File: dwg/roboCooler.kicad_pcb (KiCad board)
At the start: 2 copper layers, 60 x 72 mm, 62 parts, among them J1 CONN_01X02, J10 CONN_02X03, J11 CONN_01X04, J12 USB_A, J13 CONN_02X03, J14 CONN_02X03, J2 CONN_01X02, J3 Discovery_F407_P1, J4 CONN_01X06, J5 CONN_01X12, J6 Discovery_F407_P2, J7 CONN_02X03, J8 CONN_02X03, Q1 NMOS, Q2 NMOS, U1 SN74LV, U2 TB6549

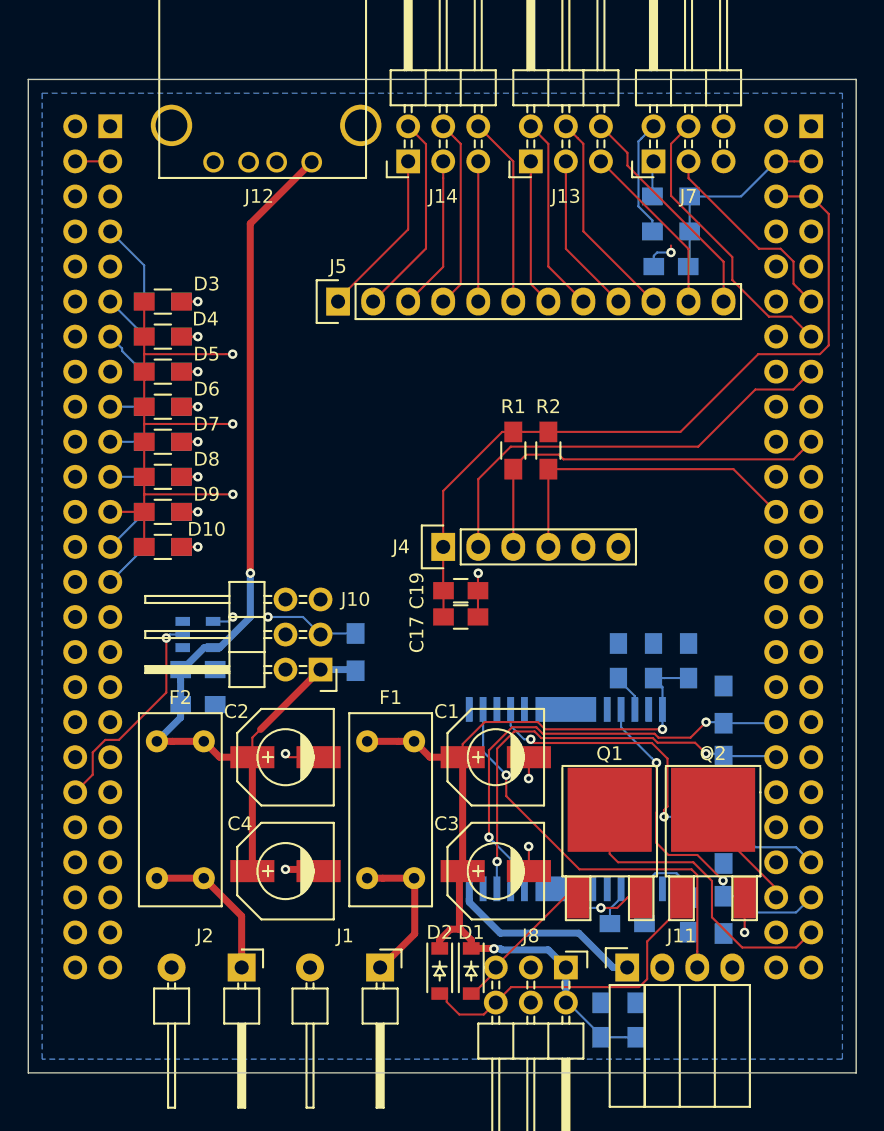
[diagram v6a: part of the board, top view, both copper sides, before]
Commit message: increased some track widths on pcb
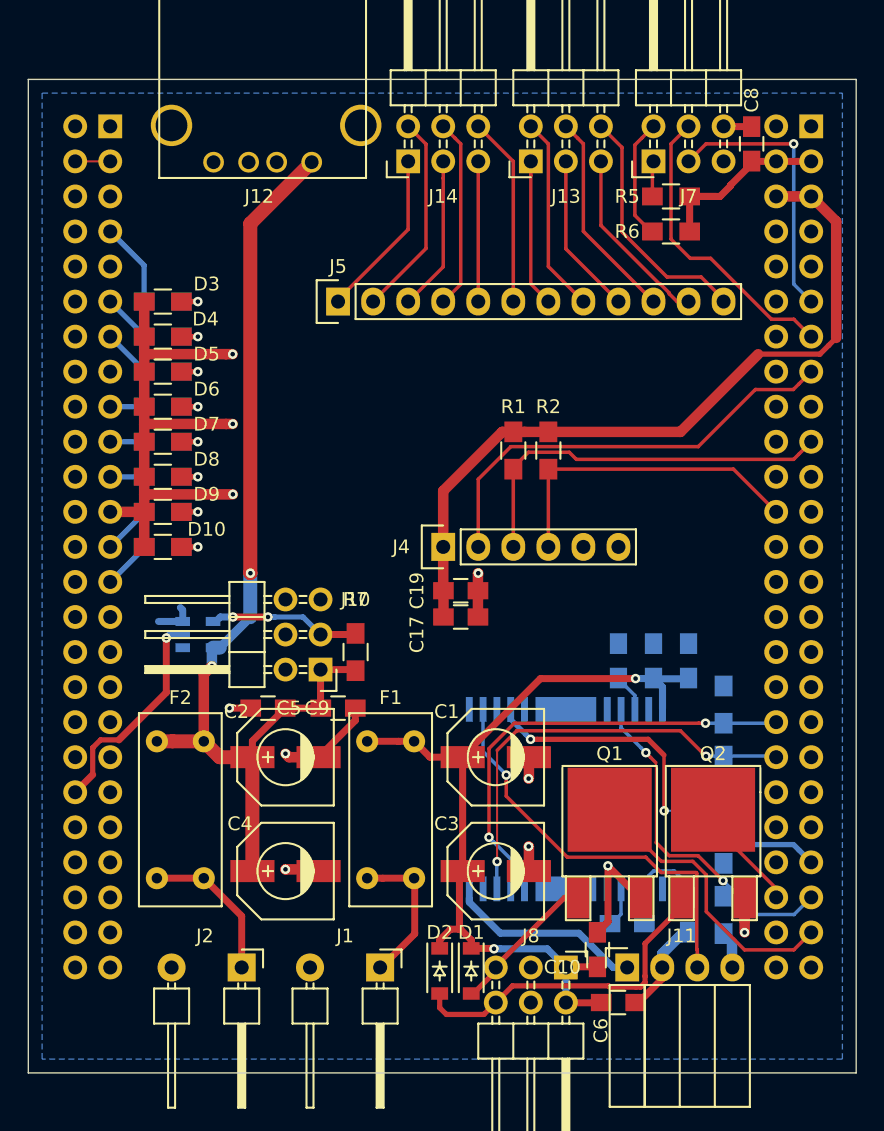
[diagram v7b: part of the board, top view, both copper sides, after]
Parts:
- C10, C5, C6, C8, C9, R5, R6, R7: moved to F.Cu
- moved C8 10.6 mm to (74.4, 26.7), turned to 90 degrees
- moved C5 10.5 mm to (44.5, 67.6)
- moved C10 5.82 mm to (63.2, 85.1)
- moved C9 5.09 mm to (39.4, 67.6), turned to 180 degrees
- moved C6 1.80 mm to (64.8, 88.9), turned to 0 degrees
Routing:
- net GND: track 64.1 -> 82.9 mm
- net HALL_1: track 14.8 -> 20.1 mm, vias 0 -> 1
- net FAN: track 22.6 -> 20.9 mm
- net CS_0: track 16.4 -> 17.8 mm
- net PUMP: track 8.25 -> 7.12 mm
- net Net-(D2-Pad2): track 23.9 -> 24.8 mm
- net HALL_2: track 20.9 -> 21.8 mm
- net MOTOR_PWM: track 29.9 -> 29.2 mm
- net MOTOR_IN1: track 33.0 -> 32.4 mm
- net +5P: track 15.1 -> 14.5 mm
- net CS_1: track 12.8 -> 13.3 mm
- net +5V: track 74.0 -> 73.8 mm, vias 1 -> 2
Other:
- net class Cap added: clearance 0.1524, trace_width 0.254, via_dia 0.6858, via_drill 0.3302
- net class Default: trace_width 0.1524 -> 0.254
- net class LEDS added: clearance 0.1524, trace_width 0.381, via_dia 0.6858, via_drill 0.3302
- net class Power added: clearance 0.1524, trace_width 0.508, via_dia 0.6858, via_drill 0.3302

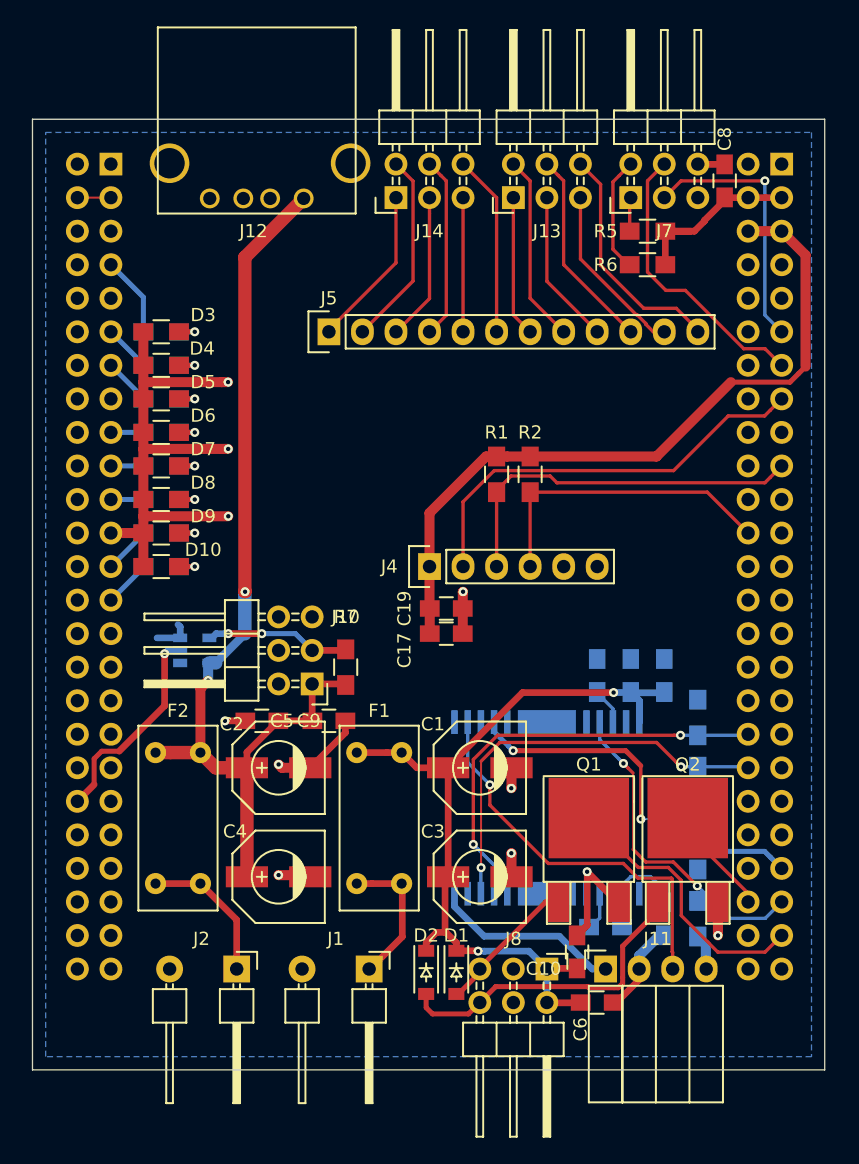
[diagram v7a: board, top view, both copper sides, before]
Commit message: added mounting holes
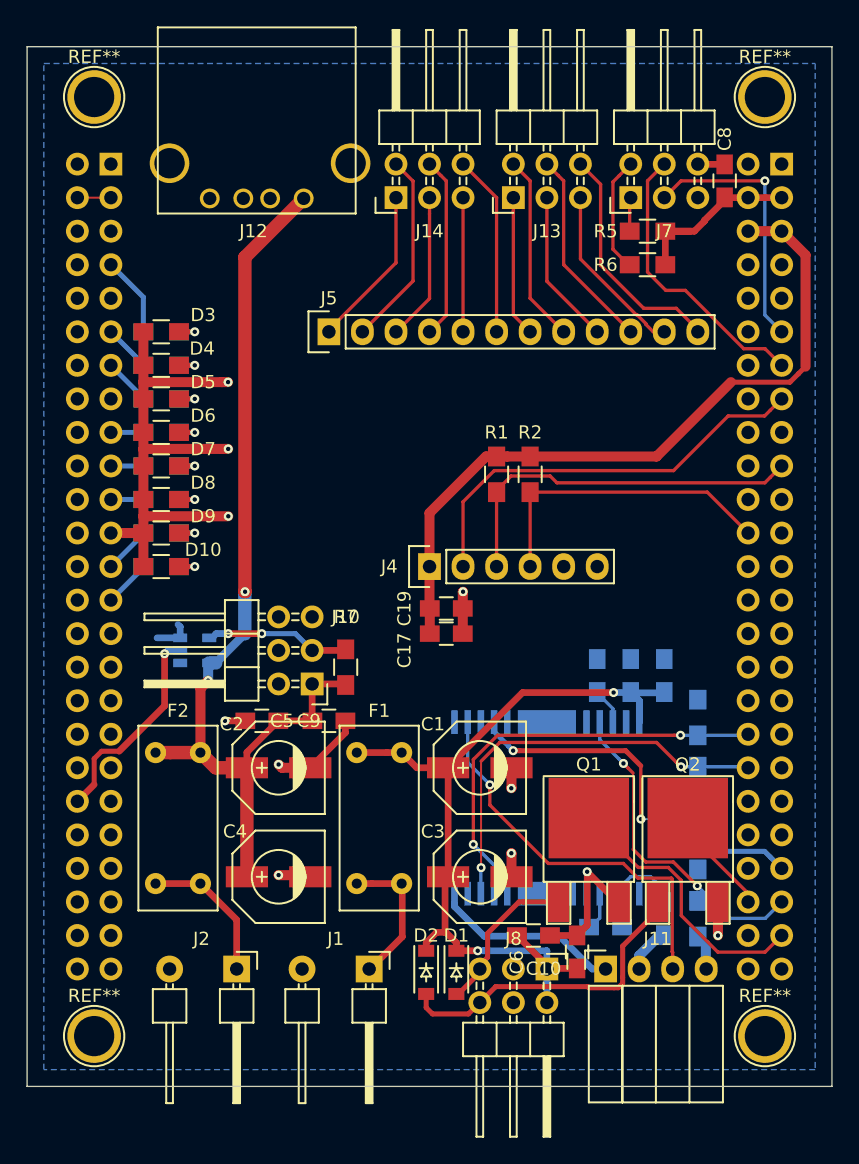
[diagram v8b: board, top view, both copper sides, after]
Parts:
- added REF**: 1pin, Connect:1pin, F.Cu at (77.5, 20.3)
- added REF**: 1pin, Connect:1pin, F.Cu at (26.7, 20.3)
- added REF**: 1pin, Connect:1pin, F.Cu at (77.5, 91.4)
- added REF**: 1pin, Connect:1pin, F.Cu at (26.7, 91.4)
- moved C6 7.01 mm to (59.9, 83.8)
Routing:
- net +12V: track 63.6 -> 65.7 mm
- net GND: track 82.9 -> 81.5 mm
- net Net-(D1-Pad2): track 10.8 -> 12.0 mm
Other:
- board size 60 x 72 mm -> 61 x 78.7 mm
